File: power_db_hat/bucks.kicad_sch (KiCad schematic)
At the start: 46 parts, among them Q6 SIS468DN, Q7 SIS468DN, U3 MAX17506ATP+T, U5 MAX17506ATP+T

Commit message: termination
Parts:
- added JP10, JP9: SolderJumper_2_Open, Jumper:SolderJumper-2_P1.3mm_Open_TrianglePad1.0x1.5mm, symbol Jumper:SolderJumper_2_Open
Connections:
- net BUCK_IN: now also JP10.2 (B), JP9.2 (B); no longer R65.1, R66.1
- new net: JP9.1 (A), R66.1
- new net: JP10.1 (A), R65.1
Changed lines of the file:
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@@
 	(wire
 		(pts
+			(xy 163.83 172.72) (xy 167.64 172.72)
+		)
+		(stroke
+			(width 0)
+			(type default)
+		)
+	)
+	(wire
+		(pts
 			(xy 120.65 134.62) (xy 120.65 137.16)
 		)
@@
 	(wire
 		(pts
-			(xy 87.63 38.1) (xy 106.68 38.1)
+			(xy 152.4 172.72) (xy 156.21 172.72)
 		)
 		(stroke
@@
 	(wire
 		(pts
-			(xy 152.4 172.72) (xy 157.48 172.72)
+			(xy 87.63 38.1) (xy 106.68 38.1)
 		)
 		(stroke
@@
 	(wire
 		(pts
+			(xy 194.31 83.82) (xy 199.39 83.82)
+		)
+		(stroke
+			(width 0)
+			(type default)
+		)
+	)
+	(wire
+		(pts
 			(xy 95.25 53.34) (xy 95.25 55.88)
 		)
@@
 	(wire
 		(pts
+			(xy 207.01 83.82) (xy 209.55 83.82)
+		)
+		(stroke
+			(width 0)
+			(type default)
+		)
+	)
+	(wire
+		(pts
 			(xy 83.82 67.31) (xy 96.52 67.31)
 		)
@@
 	(wire
 		(pts
-			(xy 194.31 83.82) (xy 199.39 83.82)
-		)
-		(stroke
-			(width 0)
-			(type default)
-		)
-	)
-	(wire
-		(pts
 			(xy 149.86 160.02) (xy 157.48 160.02)
 		)
@@
 	(hierarchical_label "BUCK_IN"
 		(shape input)
-		(at 199.39 83.82 0)
+		(at 209.55 83.82 0)
 		(effects
 			(font
@@
 	(hierarchical_label "BUCK_IN"
 		(shape input)
-		(at 157.48 172.72 0)
+		(at 167.64 172.72 0)
 		(effects
 			(font
@@
 	)
 	(symbol
+		(lib_id "Jumper:SolderJumper_2_Open")
+		(at 160.02 172.72 0)
+		(unit 1)
+		(body_style 1)
+		(exclude_from_sim no)
+		(in_bom no)
+		(on_board yes)
+		(in_pos_files yes)
+		(dnp no)
+		(property "Reference" "JP9"
+			(at 160.02 169.164 0)
+			(show_name no)
+			(do_not_autoplace no)
+			(effects
+				(font
+					(size 1.27 1.27)
+				)
+			)
+		)
+		(property "Value" "SolderJumper_2_Open"
+			(at 163.322 164.338 0)
+			(hide yes)
+			(show_name no)
+			(do_not_autoplace no)
+			(effects
+				(font
+					(size 1.27 1.27)
+				)
+			)
+		)
+		(property "Footprint" "Jumper:SolderJumper-2_P1.3mm_Open_TrianglePad1.0x1.5mm"
+			(at 160.02 172.72 0)
+			(hide yes)
+			(show_name no)
+			(do_not_autoplace no)
+			(effects
+				(font
+					(size 1.27 1.27)
+				)
+			)
+		)
+		(property "Datasheet" ""
+			(at 160.02 172.72 0)
+			(hide yes)
+			(show_name no)
+			(do_not_autoplace no)
+			(effects
+				(font
+					(size 1.27 1.27)
+				)
+			)
+		)
+		(property "Description" "Solder Jumper, 2-pole, open"
+			(at 160.02 172.72 0)
+			(hide yes)
+			(show_name no)
+			(do_not_autoplace no)
+			(effects
+				(font
+					(size 1.27 1.27)
+				)
+			)
+		)
+		(pin "1"
+		)
+		(pin "2"
+		)
+		(instances
+			(project "power_db_hat"
+				(path "/e63e39d7-6ac0-4ffd-8aa3-1841a4541b55/fd5e5e33-5dc6-45b9-b42d-1fb287c03766/e2ba82d1-535c-4903-80e9-08eeda962fab"
+					(reference "JP9")
+					(unit 1)
+				)
+			)
+		)
+	)
+	(symbol
 		(lib_id "Device:C")
 		(at 154.94 135.89 0)
@@
 					(unit 1)
 				)
+			)
+		)
+	)
+	(symbol
+		(lib_id "Jumper:SolderJumper_2_Open")
+		(at 203.2 83.82 0)
+		(unit 1)
+		(body_style 1)
+		(exclude_from_sim no)
+		(in_bom no)
+		(on_board yes)
+		(in_pos_files yes)
+		(dnp no)
+		(property "Reference" "JP10"
+			(at 203.2 80.264 0)
+			(show_name no)
+			(do_not_autoplace no)
+			(effects
+				(font
+					(size 1.27 1.27)
+				)
+			)
+		)
+		(property "Value" "SolderJumper_2_Open"
+			(at 206.502 75.438 0)
+			(hide yes)
+			(show_name no)
+			(do_not_autoplace no)
+			(effects
+				(font
+					(size 1.27 1.27)
+				)
+			)
+		)
+		(property "Footprint" "Jumper:SolderJumper-2_P1.3mm_Open_TrianglePad1.0x1.5mm"
+			(at 203.2 83.82 0)
+			(hide yes)
+			(show_name no)
+			(do_not_autoplace no)
+			(effects
+				(font
+					(size 1.27 1.27)
+				)
+			)
+		)
+		(property "Datasheet" ""
+			(at 203.2 83.82 0)
+			(hide yes)
+			(show_name no)
+			(do_not_autoplace no)
+			(effects
+				(font
+					(size 1.27 1.27)
+				)
+			)
+		)
+		(property "Description" "Solder Jumper, 2-pole, open"
+			(at 203.2 83.82 0)
+			(hide yes)
+			(show_name no)
+			(do_not_autoplace no)
+			(effects
+				(font
+					(size 1.27 1.27)
+				)
+			)
+		)
+		(pin "1"
+		)
+		(pin "2"
+		)
+		(instances
+			(project "power_db_hat"
+				(path "/e63e39d7-6ac0-4ffd-8aa3-1841a4541b55/fd5e5e33-5dc6-45b9-b42d-1fb287c03766/e2ba82d1-535c-4903-80e9-08eeda962fab"
+					(reference "JP10")
+					(unit 1)
+				)

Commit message: update
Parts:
- L1: footprint Inductor_TDK:IND_B82477G4472M000 -> IND_B82477G4472M000:IND_B82477G4472M000
- L2: footprint (none) -> IND_B82477G4472M000:IND_B82477G4472M000
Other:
- note added: "B82477G4103M000"
- note added: "B82477G4472M000"
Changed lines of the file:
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@@
 		)
 	)
+	(text "B82477G4103M000"
+		(exclude_from_sim no)
+		(at 145.034 124.46 0)
+		(effects
+			(font
+				(size 1.27 1.27)
+			)
+		)
+	)
 	(text "DNP\n"
 		(exclude_from_sim no)
@@
 		)
 	)
+	(text "B82477G4472M000"
+		(exclude_from_sim no)
+		(at 185.928 35.052 0)
+		(effects
+			(font
+				(size 1.27 1.27)
+			)
+		)
+	)
 	(junction
 		(at 172.72 43.18)
@@
 	)
 	(junction
-		(at 162.56 132.08)
-		(diameter 0)
-		(color 0 0 0 0)
-	)
-	(junction
 		(at 154.94 132.08)
 		(diameter 0)
@@
 	)
 	(junction
+		(at 162.56 132.08)
+		(diameter 0)
+		(color 0 0 0 0)
+	)
+	(junction
 		(at 120.65 137.16)
 		(diameter 0)
@@
 	(wire
 		(pts
-			(xy 162.56 132.08) (xy 196.85 132.08)
+			(xy 162.56 132.08) (xy 195.58 132.08)
 		)
 		(stroke
@@
 	(wire
 		(pts
-			(xy 92.71 43.18) (xy 106.68 43.18)
+			(xy 91.44 43.18) (xy 106.68 43.18)
 		)
 		(stroke
@@
 	(wire
 		(pts
-			(xy 92.71 45.72) (xy 92.71 43.18)
+			(xy 91.44 45.72) (xy 91.44 43.18)
 		)
 		(stroke
@@
 	(wire
 		(pts
-			(xy 87.63 45.72) (xy 92.71 45.72)
+			(xy 87.63 45.72) (xy 91.44 45.72)
 		)
 		(stroke
@@
 	)
 	(label "BUCK_OUT_12V"
-		(at 166.37 132.08 0)
+		(at 167.64 132.08 0)
 		(effects
 			(font
@@
 	(hierarchical_label "BUCK_OUT_12V"
 		(shape input)
-		(at 196.85 132.08 0)
+		(at 195.58 132.08 0)
 		(effects
 			(font
@@
 			)
 		)
-		(property "Footprint" ""
+		(property "Footprint" "IND_B82477G4472M000:IND_B82477G4472M000"
 			(at 138.43 132.08 0)
 			(hide yes)
@@
 		(dnp no)
 		(property "Reference" "C14"
-			(at 86.106 48.006 0)
+			(at 89.154 52.07 0)
 			(show_name no)
 			(do_not_autoplace no)
@@
 		)
 		(property "Value" "2.2uF"
-			(at 86.106 50.546 0)
+			(at 89.154 54.61 0)
 			(show_name no)
 			(do_not_autoplace no)
@@
 			)
 		)
-		(property "Footprint" "Inductor_TDK:IND_B82477G4472M000"
+		(property "Footprint" "IND_B82477G4472M000:IND_B82477G4472M000"
 			(at 180.34 43.18 0)
 			(hide yes)

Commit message: lol
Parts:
- L1: footprint IND_B82477G4472M000:IND_B82477G4472M000 -> B82477G4472M000:IND_B82477G4472M000
- L2: footprint IND_B82477G4472M000:IND_B82477G4472M000 -> Inductor_SMD:L_TDK_VLS6045EX_VLS6045AF
- Q6, Q7: footprint Package_SO:Vishay_PowerPAK_1212-8_Single -> SiS468DN:Vishay_PowerPAK_1212-8_Single
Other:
- note added: "VLS6045EX-100M"
- note removed: "B82477G4103M000"
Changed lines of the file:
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@@
 		)
 	)
-	(text "B82477G4103M000"
+	(text "VLS6045EX-100M"
 		(exclude_from_sim no)
-		(at 145.034 124.46 0)
+		(at 141.986 123.698 0)
 		(effects
 			(font
@@
 			)
 		)
-		(property "Footprint" "Package_SO:Vishay_PowerPAK_1212-8_Single"
+		(property "Footprint" "SiS468DN:Vishay_PowerPAK_1212-8_Single"
 			(at 133.35 118.11 0)
 			(hide yes)
@@
 			)
 		)
-		(property "Footprint" "IND_B82477G4472M000:IND_B82477G4472M000"
+		(property "Footprint" "Inductor_SMD:L_TDK_VLS6045EX_VLS6045AF"
 			(at 138.43 132.08 0)
 			(hide yes)
@@
 			)
 		)
-		(property "Footprint" "IND_B82477G4472M000:IND_B82477G4472M000"
+		(property "Footprint" "B82477G4472M000:IND_B82477G4472M000"
 			(at 180.34 43.18 0)
 			(hide yes)
@@
 			)
 		)
-		(property "Footprint" "Package_SO:Vishay_PowerPAK_1212-8_Single"
+		(property "Footprint" "SiS468DN:Vishay_PowerPAK_1212-8_Single"
 			(at 175.26 29.21 0)
 			(hide yes)

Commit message: LMAO
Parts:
- added R33, R34: 10m, Resistor_SMD:R_2512_6332Metric_Pad1.40x3.35mm_HandSolder, symbol Device:R_US
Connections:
- net 5V_SNS+: now reaches C16.2, Q7.1 (D), U3.17 (LX), U3.18 (LX), U3.19 (LX)
- net 5V_SNS+: now also R34.2; no longer L1.1
- net 12V_SNS+: now reaches C37.2, Q6.1 (D), U5.17 (LX), U5.18 (LX), U5.19 (LX)
- net 12V_SNS+: now also R33.2; no longer L2.1
- new net 12V_SNS-: L2.1, R33.1
- new net 5V_SNS-: L1.1, R34.1
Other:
- moved on the sheet: C17, C27, C28, C39, C41, C43, L1, L2

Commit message: damo was here
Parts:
- removed JP10, JP9: SolderJumper_2_Open, Jumper:SolderJumper-2_P1.3mm_Open_TrianglePad1.0x1.5mm, symbol Jumper:SolderJumper_2_Open
- removed R30, R38: 10k, Resistor_SMD:R_0603_1608Metric_Pad0.98x0.95mm_HandSolder, symbol Device:R_US
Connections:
- net BUCK_OUT is gone; now on net 5V_SNS-: R19.2
- net 12V_SNS+: now also L2.2; no longer C37.2, Q6.1 (D), U5.17 (LX), U5.18 (LX), U5.19 (LX)
- net 12V_SNS-: now also C39.1, C41.1, C43.1, R35.1, R42.2; no longer L2.1
- net 5V_SNS+: now also L1.2; no longer C16.2, Q7.1 (D), U3.17 (LX), U3.18 (LX), U3.19 (LX)
- net 5V_SNS-: now also C17.1, C27.1, C28.1, R22.1; no longer L1.1
- net BUCK_IN: now also R65.1, R66.1
- removed net BUCK_OUT_12V: C39.1, C41.1, C43.1, L2.2, R35.1, R42.2
- removed net BUCK_OUT_5V: C17.1, C27.1, C28.1, L1.2, R22.1
- new net: C16.2, L1.1, Q7.1 (D), U3.17 (LX), U3.18 (LX), U3.19 (LX)
- new net: C37.2, L2.1, Q6.1 (D), U5.17 (LX), U5.18 (LX), U5.19 (LX)
- no-connect marks 6 -> 8
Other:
- moved on the sheet: L2, R34

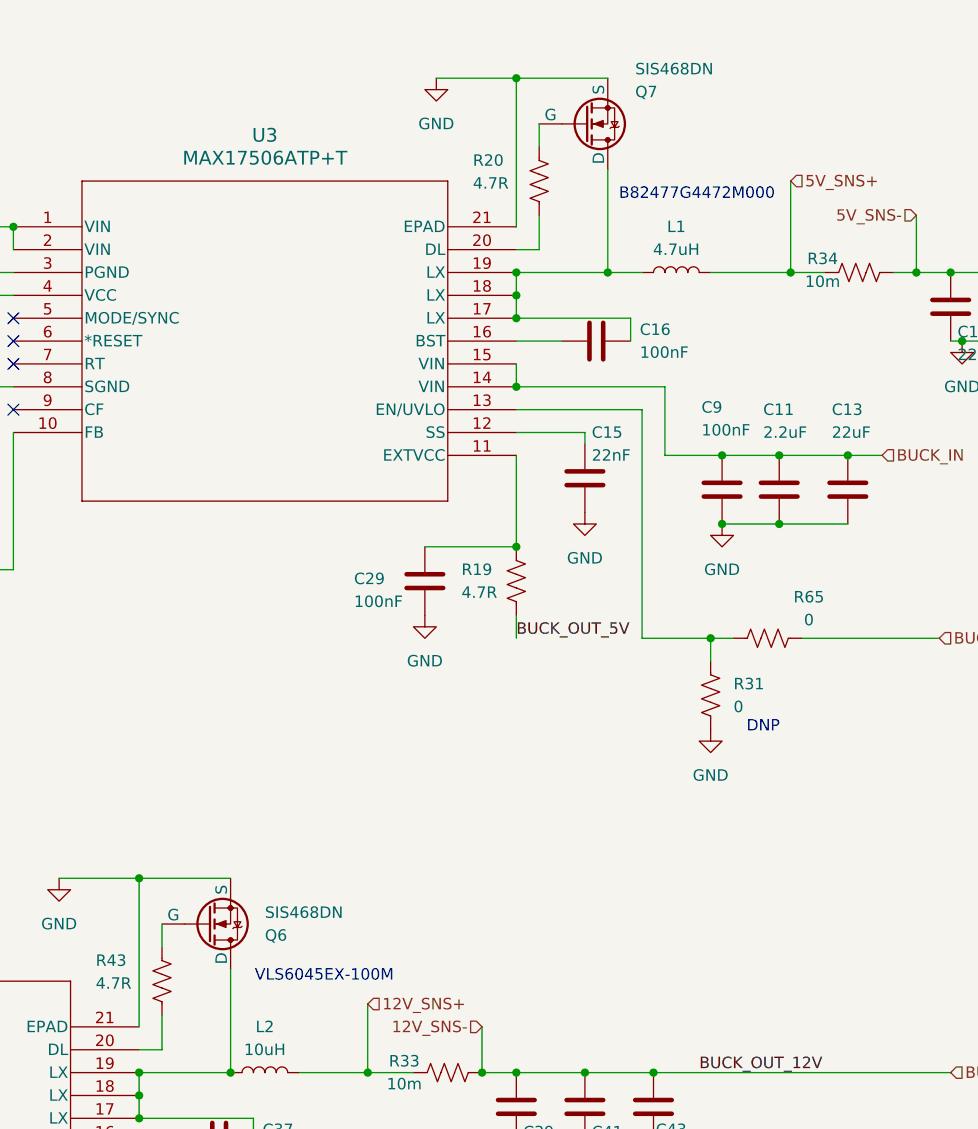
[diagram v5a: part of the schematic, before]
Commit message: updated 3d models for power
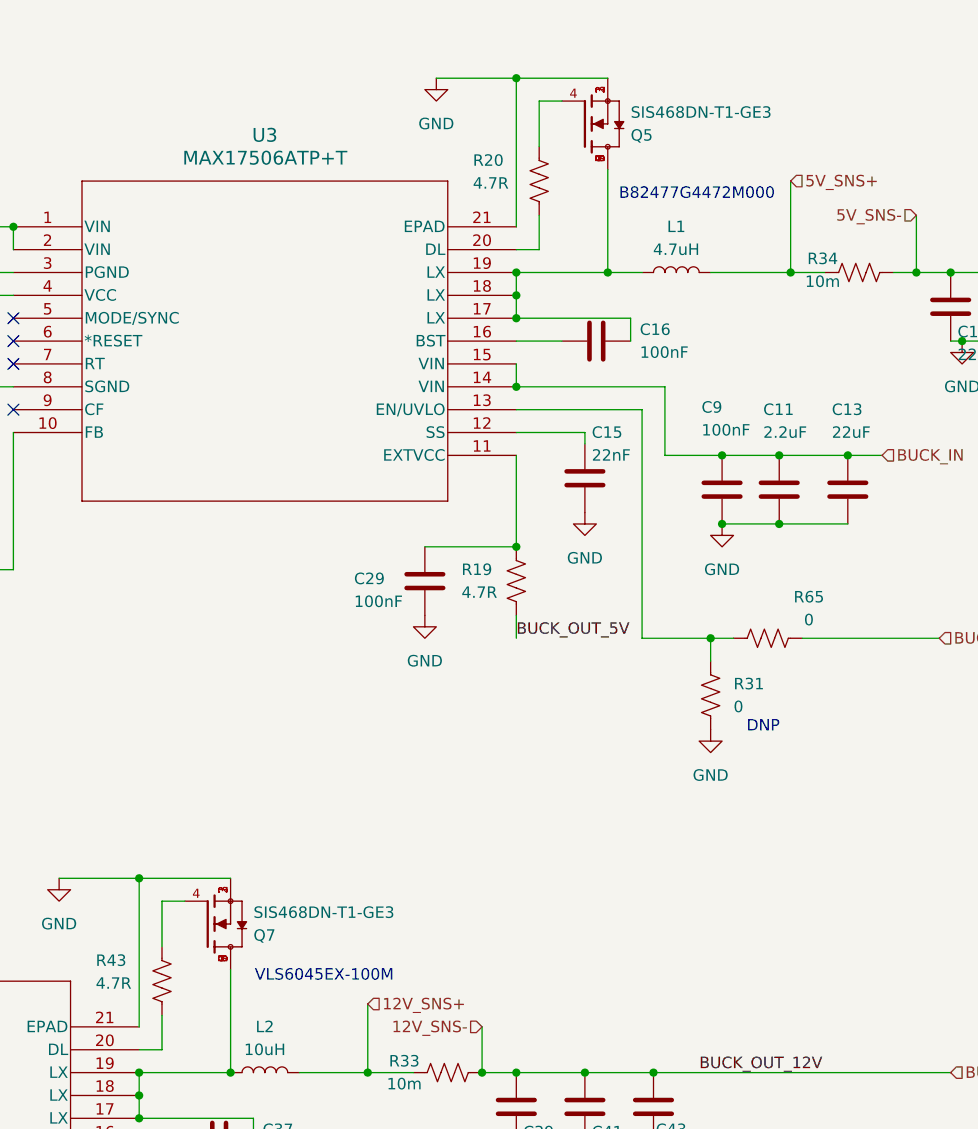
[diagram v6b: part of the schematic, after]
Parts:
- removed Q6, Q7: SIS468DN, SiS468DN:Vishay_PowerPAK_1212-8_Single, symbol Simulation_SPICE:NMOS
- added Q5, Q7: SIS468DN-T1-GE3, SiS468DN-T1-GE3:VISHAY_SIS468DN-T1-GE3, symbol SiS468DN-T1-GE3:SIS468DN-T1-GE3
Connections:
- net GND: now also Q5.1, Q5.2, Q5.3, Q7.1, Q7.2, Q7.3
- net at C16.2, L1.1, U3.17 (LX)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: now also Q5.5, Q5.6, Q5.7, Q5.8, Q5.9
- net at C37.2, L2.1, U5.17 (LX)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: now also Q7.5, Q7.6, Q7.7, Q7.8, Q7.9
- net at R43.1: now also Q7.4
- net at R20.1: now also Q5.4
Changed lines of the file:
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@@
 	(wire
 		(pts
+			(xy 123.19 113.03) (xy 123.19 118.11)
+		)
+		(stroke
+			(width 0)
+			(type default)
+		)
+	)
+	(wire
+		(pts
 			(xy 191.77 71.12) (xy 199.39 71.12)
 		)
@@
 	(wire
 		(pts
+			(xy 125.73 113.03) (xy 123.19 113.03)
+		)
+		(stroke
+			(width 0)
+			(type default)
+		)
+	)
+	(wire
+		(pts
 			(xy 120.65 132.08) (xy 130.81 132.08)
 		)
@@
 	(wire
 		(pts
+			(xy 167.64 24.13) (xy 165.1 24.13)
+		)
+		(stroke
+			(width 0)
+			(type default)
+		)
+	)
+	(wire
+		(pts
 			(xy 176.53 58.42) (xy 176.53 83.82)
 		)
@@
 	(wire
 		(pts
-			(xy 123.19 115.57) (xy 123.19 118.11)
+			(xy 165.1 24.13) (xy 165.1 29.21)
 		)
 		(stroke
@@
 	(wire
 		(pts
-			(xy 165.1 26.67) (xy 165.1 29.21)
-		)
-		(stroke
-			(width 0)
-			(type default)
-		)
-	)
-	(wire
-		(pts
 			(xy 64.77 165.1) (xy 64.77 149.86)
 		)
@@
 	)
 	(symbol
-		(lib_id "Simulation_SPICE:NMOS")
-		(at 128.27 115.57 0)
-		(mirror x)
-		(unit 1)
-		(body_style 1)
-		(exclude_from_sim no)
-		(in_bom yes)
-		(on_board yes)
-		(in_pos_files yes)
-		(dnp no)
-		(property "Reference" "Q6"
-			(at 134.62 116.8401 0)
-			(show_name no)
-			(do_not_autoplace no)
-			(effects
-				(font
-					(size 1.27 1.27)
-				)
-				(justify left)
-			)
-		)
-		(property "Value" "SIS468DN"
-			(at 134.62 114.3001 0)
-			(show_name no)
-			(do_not_autoplace no)
-			(effects
-				(font
-					(size 1.27 1.27)
-				)
-				(justify left)
-			)
-		)
-		(property "Footprint" "SiS468DN:Vishay_PowerPAK_1212-8_Single"
-			(at 133.35 118.11 0)
-			(hide yes)
-			(show_name no)
-			(do_not_autoplace no)
-			(effects
-				(font
-					(size 1.27 1.27)
-				)
-			)
-		)
-		(property "Datasheet" "https://ngspice.sourceforge.io/docs/ngspice-html-manual/manual.xhtml#cha_MOSFETs"
-			(at 128.27 102.87 0)
-			(hide yes)
-			(show_name no)
-			(do_not_autoplace no)
-			(effects
-				(font
-					(size 1.27 1.27)
-				)
-			)
-		)
-		(property "Description" "N-MOSFET transistor, drain/source/gate"
-			(at 128.27 115.57 0)
-			(hide yes)
-			(show_name no)
-			(do_not_autoplace no)
-			(effects
-				(font
-					(size 1.27 1.27)
-				)
-			)
-		)
-		(property "Sim.Device" "NMOS"
-			(at 128.27 98.425 0)
-			(hide yes)
-			(show_name no)
-			(do_not_autoplace no)
-			(effects
-				(font
-					(size 1.27 1.27)
-				)
-			)
-		)
-		(property "Sim.Type" "VDMOS"
-			(at 128.27 96.52 0)
-			(hide yes)
-			(show_name no)
-			(do_not_autoplace no)
-			(effects
-				(font
-					(size 1.27 1.27)
-				)
-			)
-		)
-		(property "Sim.Pins" "1=D 2=G 3=S"
-			(at 128.27 100.33 0)
-			(hide yes)
-			(show_name no)
-			(do_not_autoplace no)
-			(effects
-				(font
-					(size 1.27 1.27)
-				)
-			)
-		)
-		(pin "1"
-		)
-		(pin "3"
-		)
-		(pin "2"
-		)
-		(instances
-			(project "power_db_hat"
-				(path "/e63e39d7-6ac0-4ffd-8aa3-1841a4541b55/fd5e5e33-5dc6-45b9-b42d-1fb287c03766/e2ba82d1-535c-4903-80e9-08eeda962fab"
-					(reference "Q6")
-					(unit 1)
-				)
-			)
-		)
-	)
-	(symbol
 		(lib_id "Device:C")
 		(at 80.01 41.91 0)
@@
 	)
 	(symbol
-		(lib_id "Simulation_SPICE:NMOS")
-		(at 170.18 26.67 0)
+		(lib_id "SiS468DN-T1-GE3:SIS468DN-T1-GE3")
+		(at 129.54 115.57 0)
 		(mirror x)
 		(unit 1)
@@
 		(dnp no)
 		(property "Reference" "Q7"
-			(at 175.768 23.114 0)
+			(at 133.35 116.8401 0)
 			(show_name no)
 			(do_not_autoplace no)
@@
 			)
 		)
-		(property "Value" "SIS468DN"
-			(at 175.768 20.574 0)
+		(property "Value" "SIS468DN-T1-GE3"
+			(at 133.35 114.3001 0)
 			(show_name no)
 			(do_not_autoplace no)
@@
 			)
 		)
-		(property "Footprint" "SiS468DN:Vishay_PowerPAK_1212-8_Single"
-			(at 175.26 29.21 0)
+		(property "Footprint" "SiS468DN-T1-GE3:VISHAY_SIS468DN-T1-GE3"
+			(at 129.54 115.57 0)
 			(hide yes)
 			(show_name no)
@@
 					(size 1.27 1.27)
 				)
+				(justify bottom)
 			)
 		)
-		(property "Datasheet" "https://ngspice.sourceforge.io/docs/ngspice-html-manual/manual.xhtml#cha_MOSFETs"
-			(at 170.18 13.97 0)
+		(property "Datasheet" ""
+			(at 129.54 115.57 0)
 			(hide yes)
 			(show_name no)
@@
 			)
 		)
-		(property "Description" "N-MOSFET transistor, drain/source/gate"
-			(at 170.18 26.67 0)
+		(property "Description" ""
+			(at 129.54 115.57 0)
 			(hide yes)
 			(show_name no)
@@
 			)
 		)
-		(property "Sim.Device" "NMOS"
-			(at 170.18 9.525 0)
+		(property "PARTREV" "A"
+			(at 129.54 115.57 0)
 			(hide yes)
 			(show_name no)
@@
 					(size 1.27 1.27)
 				)
+				(justify bottom)
 			)
 		)
-		(property "Sim.Type" "VDMOS"
-			(at 170.18 7.62 0)
+		(property "MANUFACTURER" "VISHAY"
+			(at 129.54 115.57 0)
 			(hide yes)
 			(show_name no)
@@
 					(size 1.27 1.27)
 				)
+				(justify bottom)
 			)
 		)
-		(property "Sim.Pins" "1=D 2=G 3=S"
-			(at 170.18 11.43 0)
+		(property "STANDARD" "MANUFACTURER RECOMMENDATIONS"
+			(at 129.54 115.57 0)
 			(hide yes)
 			(show_name no)
@@
 					(size 1.27 1.27)
 				)
+				(justify bottom)
 			)
 		)
+		(pin "3"
+		)
+		(pin "6"
+		)
 		(pin "1"
 		)
+		(pin "2"
+		)
+		(pin "4"
+		)
+		(pin "5"
+		)
+		(pin "7"
+		)
+		(pin "9"
+		)
+		(pin "8"
+		)
+		(instances
+			(project "power_db_hat"
+				(path "/e63e39d7-6ac0-4ffd-8aa3-1841a4541b55/fd5e5e33-5dc6-45b9-b42d-1fb287c03766/e2ba82d1-535c-4903-80e9-08eeda962fab"
+					(reference "Q7")
+					(unit 1)
+				)
+			)
+		)
+	)
+	(symbol
+		(lib_id "SiS468DN-T1-GE3:SIS468DN-T1-GE3")
+		(at 171.45 26.67 0)
+		(mirror x)
+		(unit 1)
+		(body_style 1)
+		(exclude_from_sim no)
+		(in_bom yes)
+		(on_board yes)
+		(in_pos_files yes)
+		(dnp no)
+		(property "Reference" "Q5"
+			(at 175.26 27.9401 0)
+			(show_name no)
+			(do_not_autoplace no)
+			(effects
+				(font
+					(size 1.27 1.27)
+				)
+				(justify left)
+			)
+		)
+		(property "Value" "SIS468DN-T1-GE3"
+			(at 175.26 25.4001 0)
+			(show_name no)
+			(do_not_autoplace no)
+			(effects
+				(font
+					(size 1.27 1.27)
+				)
+				(justify left)
+			)
+		)
+		(property "Footprint" "SiS468DN-T1-GE3:VISHAY_SIS468DN-T1-GE3"
+			(at 171.45 26.67 0)
+			(hide yes)
+			(show_name no)
+			(do_not_autoplace no)
+			(effects
+				(font
+					(size 1.27 1.27)
+				)
+				(justify bottom)
+			)
+		)
+		(property "Datasheet" ""
+			(at 171.45 26.67 0)
+			(hide yes)
+			(show_name no)
+			(do_not_autoplace no)
+			(effects
+				(font
+					(size 1.27 1.27)
+				)
+			)
+		)
+		(property "Description" ""
+			(at 171.45 26.67 0)
+			(hide yes)
+			(show_name no)
+			(do_not_autoplace no)
+			(effects
+				(font
+					(size 1.27 1.27)
+				)
+			)
+		)
+		(property "PARTREV" "A"
+			(at 171.45 26.67 0)
+			(hide yes)
+			(show_name no)
+			(do_not_autoplace no)
+			(effects
+				(font
+					(size 1.27 1.27)
+				)
+				(justify bottom)
+			)
+		)
+		(property "MANUFACTURER" "VISHAY"
+			(at 171.45 26.67 0)
+			(hide yes)
+			(show_name no)
+			(do_not_autoplace no)
+			(effects
+				(font
+					(size 1.27 1.27)
+				)
+				(justify bottom)
+			)
+		)
+		(property "STANDARD" "MANUFACTURER RECOMMENDATIONS"
+			(at 171.45 26.67 0)
+			(hide yes)
+			(show_name no)
+			(do_not_autoplace no)
+			(effects
+				(font
+					(size 1.27 1.27)
+				)
+				(justify bottom)
+			)
+		)
 		(pin "3"
 		)
+		(pin "6"
+		)
+		(pin "1"
+		)
 		(pin "2"
 		)
+		(pin "4"
+		)
+		(pin "5"
+		)
+		(pin "7"
+		)
+		(pin "9"
+		)
+		(pin "8"
+		)
 		(instances
 			(project "power_db_hat"
 				(path "/e63e39d7-6ac0-4ffd-8aa3-1841a4541b55/fd5e5e33-5dc6-45b9-b42d-1fb287c03766/e2ba82d1-535c-4903-80e9-08eeda962fab"
-					(reference "Q7")
+					(reference "Q5")
 					(unit 1)
 				)

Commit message: working on BOM
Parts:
- C13, C8: footprint Capacitor_SMD:C_0603_1608Metric_Pad1.08x0.95mm_HandSolder -> Capacitor_SMD:C_0805_2012Metric_Pad1.18x1.45mm_HandSolder
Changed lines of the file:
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@@
 			)
 		)
-		(property "Footprint" "Capacitor_SMD:C_0603_1608Metric_Pad1.08x0.95mm_HandSolder"
+		(property "Footprint" "Capacitor_SMD:C_0805_2012Metric_Pad1.18x1.45mm_HandSolder"
 			(at 200.3552 71.12 0)
 			(hide yes)
@@
 			)
 		)
-		(property "Footprint" "Capacitor_SMD:C_0603_1608Metric_Pad1.08x0.95mm_HandSolder"
+		(property "Footprint" "Capacitor_SMD:C_0805_2012Metric_Pad1.18x1.45mm_HandSolder"
 			(at 88.5952 45.72 0)
 			(hide yes)
